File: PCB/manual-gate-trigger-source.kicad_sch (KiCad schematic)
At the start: 55 parts

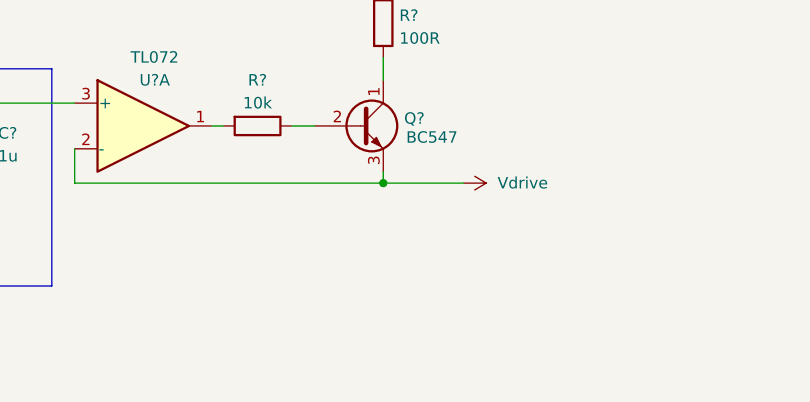
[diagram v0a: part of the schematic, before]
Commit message: :bug: Fix output ripple  by adding a filter cap
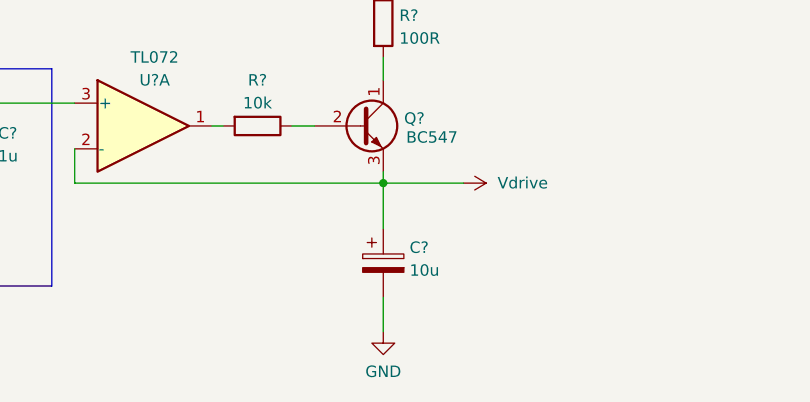
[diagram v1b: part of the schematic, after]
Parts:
- added C?: 10u, symbol Device:C_Polarized
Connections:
- net GND: now also C?.2
- net Vdrive: now also C?.1
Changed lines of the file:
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@@
+    (stroke (width 0) (type default) (color 0 0 0 0))
+  )
+  (wire (pts (xy 116.84 187.96) (xy 116.84 191.77))
     (stroke (width 0) (type default) (color 0 0 0 0))
   )
@@
   (polyline (pts (xy 78.74 53.34) (xy 78.74 55.88))
     (stroke (width 0) (type solid) (color 0 0 0 0))
+  )
+  (wire (pts (xy 116.84 175.26) (xy 116.84 180.34))
+    (stroke (width 0) (type default) (color 0 0 0 0))
   )
   (wire (pts (xy 73.66 58.42) (xy 76.2 58.42))
@@
     (pin "2")
   )
+  (symbol (lib_id "power:GND") (at 116.84 191.77 0) (unit 1)
+    (in_bom yes) (on_board yes) (fields_autoplaced)
+    (property "Reference" "#PWR?" (id 0) (at 116.84 198.12 0)
+      (effects (font (size 1.27 1.27)) hide)
+    )
+    (property "Value" "GND" (id 1) (at 116.84 196.2134 0))
+    (property "Footprint" "" (id 2) (at 116.84 191.77 0)
+      (effects (font (size 1.27 1.27)) hide)
+    )
+    (property "Datasheet" "" (id 3) (at 116.84 191.77 0)
+      (effects (font (size 1.27 1.27)) hide)
+    )
+    (pin "1")
+  )
   (symbol (lib_id "Amplifier_Operational:TL072") (at 250.19 138.43 0) (unit 3)
     (in_bom yes) (on_board yes) (fields_autoplaced)
@@
     (pin "3")
   )
+  (symbol (lib_id "Device:C_Polarized") (at 116.84 184.15 0) (unit 1)
+    (in_bom yes) (on_board yes) (fields_autoplaced)
+    (property "Reference" "C?" (id 0) (at 119.761 182.4263 0)
+      (effects (font (size 1.27 1.27)) (justify left))
+    )
+    (property "Value" "10u" (id 1) (at 119.761 184.9632 0)
+      (effects (font (size 1.27 1.27)) (justify left))
+    )
+    (property "Footprint" "" (id 2) (at 117.8052 187.96 0)
+      (effects (font (size 1.27 1.27)) hide)
+    )
+    (property "Datasheet" "~" (id 3) (at 116.84 184.15 0)
+      (effects (font (size 1.27 1.27)) hide)
+    )
+    (pin "1")
+    (pin "2")
+  )
   (symbol (lib_id "Connector:AudioJack2_Ground_SwitchT") (at 269.24 78.74 0) (mirror y) (unit 1)
     (in_bom yes) (on_board yes) (fields_autoplaced)
@@
       (reference "#PWR?") (unit 1) (value "+12V") (footprint "")
     )
+    (path "/56bf08a9-5d34-4a27-9be5-6af55092c433"
+      (reference "#PWR?") (unit 1) (value "GND") (footprint "")
+    )
     (path "/579aed09-7d4a-404f-9da3-4594f8725f68"
       (reference "#PWR?") (unit 1) (value "GND") (footprint "")
@@
       (reference "C?") (unit 1) (value "2u2") (footprint "")
     )
+    (path "/d21e2ec8-6a0c-45ba-a5a2-590471f5aac9"
+      (reference "C?") (unit 1) (value "10u") (footprint "")
+    )
     (path "/ec4efcae-bec6-4319-80bb-70e4cc9534ec"

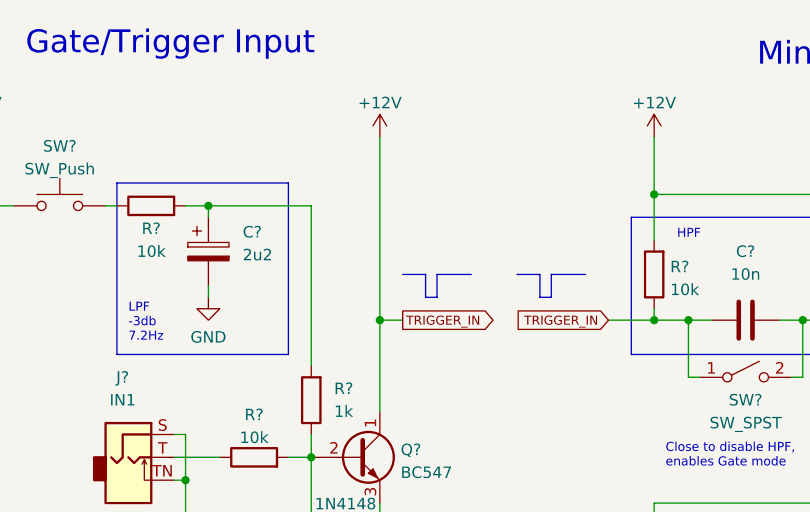
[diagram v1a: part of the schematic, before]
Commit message: :bug: Fix missing collector resistor on input transistor
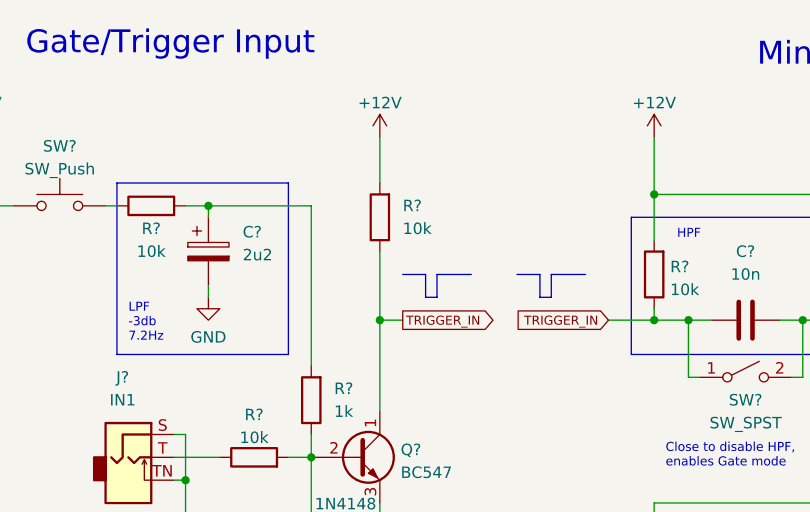
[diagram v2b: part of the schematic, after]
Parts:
- added R?: 10k, symbol Device:R
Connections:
- net +12V: now also R?.2; no longer C?.1, Q?.1 (C), R?.1, SW?.1 (A)
- new net TRIGGER_IN: C?.1, Q?.1 (C), R?.1, R?.1, SW?.1 (A)
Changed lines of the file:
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@@
+    (stroke (width 0) (type default) (color 0 0 0 0))
+  )
+  (wire (pts (xy 73.66 50.8) (xy 73.66 58.42))
     (stroke (width 0) (type default) (color 0 0 0 0))
   )
@@
     (stroke (width 0) (type default) (color 0 0 0 0))
   )
-  (wire (pts (xy 73.66 38.1) (xy 73.66 58.42))
+  (wire (pts (xy 73.66 38.1) (xy 73.66 43.18))
     (stroke (width 0) (type default) (color 0 0 0 0))
   )
@@
     )
     (pin "1")
+  )
+  (symbol (lib_id "Device:R") (at 73.66 46.99 180) (unit 1)
+    (in_bom yes) (on_board yes)
+    (property "Reference" "R?" (id 0) (at 76.2 45.7199 0)
+      (effects (font (size 1.27 1.27)) (justify right))
+    )
+    (property "Value" "10k" (id 1) (at 76.2 48.26 0)
+      (effects (font (size 1.27 1.27)) (justify right))
+    )
+    (property "Footprint" "" (id 2) (at 75.438 46.99 90)
+      (effects (font (size 1.27 1.27)) hide)
+    )
+    (property "Datasheet" "~" (id 3) (at 73.66 46.99 0)
+      (effects (font (size 1.27 1.27)) hide)
+    )
+    (pin "1")
+    (pin "2")
   )
   (symbol (lib_id "Device:R") (at 66.04 166.37 270) (unit 1)
@@
       (reference "R?") (unit 1) (value "10k") (footprint "")
     )
+    (path "/0fb9e7ee-f45c-4834-b0b9-1c6b51c3ecb8"
+      (reference "R?") (unit 1) (value "10k") (footprint "")
+    )

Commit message: :hammer: separate input into manual and CV
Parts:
- removed R?: 1k, symbol Device:R
- added R? (x2): 10k, symbol Device:R
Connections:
- net +12V: now also R?.2; no longer SW?.1
- net GND: now also R?.1
- net TRIGGER_IN: now also C?.1, R?.2, R?.1
- new net: R?.2, SW?.1
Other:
- note added: "CV Input"
- note added: "Manual Input"
- note removed: "Gate/Trigger Input"
- moved on the sheet: C?, D?, J?, Q?, R?, SW?

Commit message: :sparkles: Set MX footprint for manual switch
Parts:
- SW?: footprint (none) -> Button_Switch_Keyboard:SW_Cherry_MX_1.00u_PCB
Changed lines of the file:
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@@
     (property "Reference" "SW?" (id 0) (at 29.21 34.0192 0))
     (property "Value" "SW_Push" (id 1) (at 29.21 36.5561 0))
-    (property "Footprint" "" (id 2) (at 29.21 35.56 0)
+    (property "Footprint" "Button_Switch_Keyboard:SW_Cherry_MX_1.00u_PCB" (id 2) (at 29.21 35.56 0)
       (effects (font (size 1.27 1.27)) hide)
     )
@@
     )
     (path "/9bfdf296-af5e-4848-b739-c38d7b9b918f"
-      (reference "SW?") (unit 1) (value "SW_Push") (footprint "")
+      (reference "SW?") (unit 1) (value "SW_Push") (footprint "Button_Switch_Keyboard:SW_Cherry_MX_1.00u_PCB")
     )
     (path "/a4fc9fae-2c82-47bd-aa1f-2cb48ede91d0"

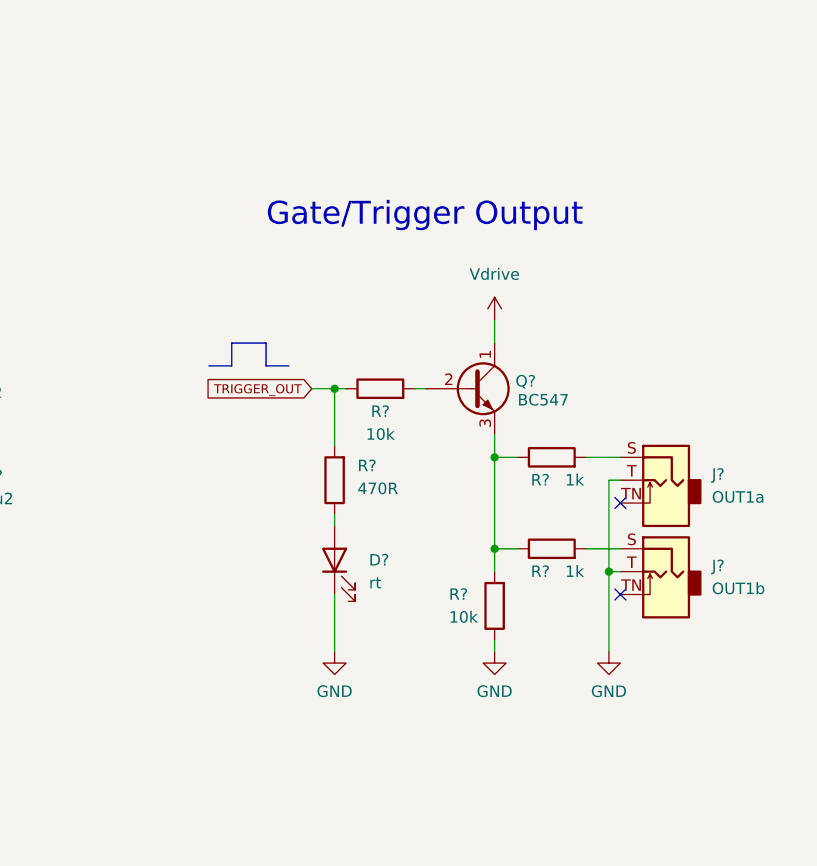
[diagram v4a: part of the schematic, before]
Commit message: :art: Replace output by push-pull configuration
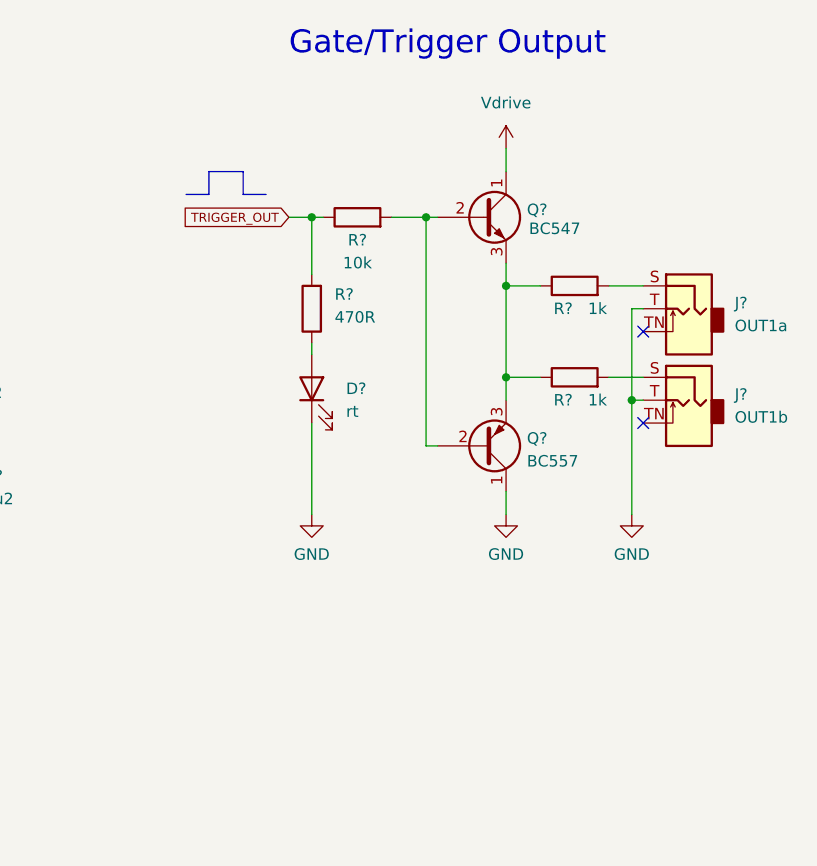
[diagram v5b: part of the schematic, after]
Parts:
- removed D?: rt, symbol Device:LED
- removed J?: OUT1a, Connector_Audio:Jack_3.5mm_QingPu_WQP-PJ398SM_Vertical_CircularHoles, symbol Connector:AudioJack2_Ground_SwitchT
- removed J?: OUT1b, Connector_Audio:Jack_3.5mm_QingPu_WQP-PJ398SM_Vertical_CircularHoles, symbol Connector:AudioJack2_Ground_SwitchT
- removed Q?: BC547, Package_TO_SOT_THT:TO-92_Inline, symbol Transistor_BJT:BC547
- removed R?: 470R, symbol Device:R
- removed R? (x2): 10k, symbol Device:R
- removed R? (x2): 1k, symbol Device:R
- added D?: rt, symbol Device:LED
- added J?: OUT1a, Connector_Audio:Jack_3.5mm_QingPu_WQP-PJ398SM_Vertical_CircularHoles, symbol Connector:AudioJack2_Ground_SwitchT
- added J?: OUT1b, Connector_Audio:Jack_3.5mm_QingPu_WQP-PJ398SM_Vertical_CircularHoles, symbol Connector:AudioJack2_Ground_SwitchT
- added Q?: BC547, Package_TO_SOT_THT:TO-92_Inline, symbol Transistor_BJT:BC547
- added Q?: BC557, Package_TO_SOT_THT:TO-92_Inline, symbol Transistor_BJT:BC557
- added R?: 470R, symbol Device:R
- added R? (x2): 1k, symbol Device:R
- added R?: 10k, symbol Device:R
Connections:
- net GND: now also D?.1 (K), J?.T, J?.T, Q?.1 (C)
- net TRIGGER_OUT: now also R?.1, R?.2
- net Vdrive: now also Q?.1 (C)
- new net: J?.S, R?.2 (x2)
- new net: D?.2 (A), R?.1
- new net: Q?.2 (B), Q?.2 (B), R?.2
- new net: Q?.3 (E), Q?.3 (E), R?.1, R?.1
